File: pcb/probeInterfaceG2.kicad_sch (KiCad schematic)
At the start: 41 parts

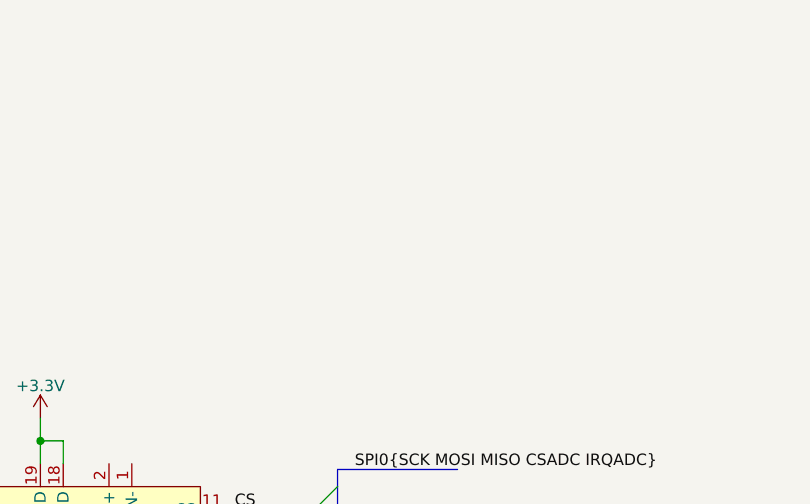
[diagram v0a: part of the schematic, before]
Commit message: Added some design hints
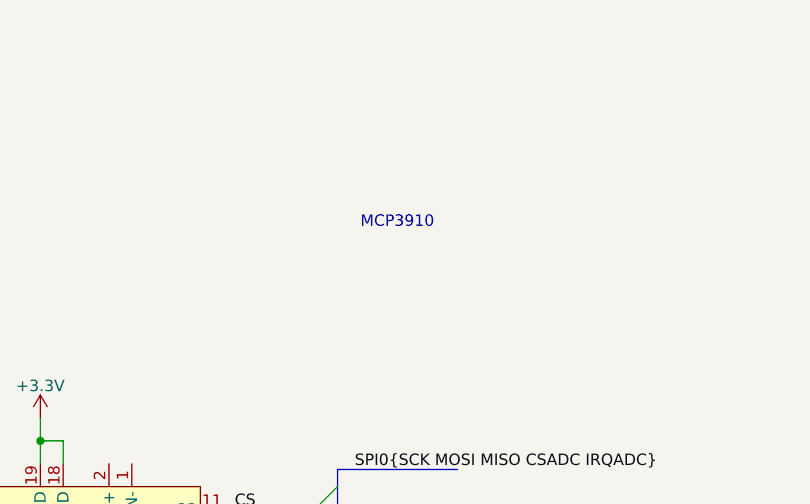
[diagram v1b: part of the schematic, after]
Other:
- note added: "MCP3910"

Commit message: updated schematics for bipolar supply of opamps
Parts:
- removed C?: 100n, symbol Device:C
- removed C? (x2): 220n, symbol Device:C
- removed R? (x2): 220, symbol Device:R
- removed U? (x5): 74HCT4052, symbol Analog_Switch:CD4052B
- removed U? (x2): 74HC595, symbol 74xx:74HC595
- removed U? (x3): LM358, symbol Amplifier_Operational:LM358
- added C?: 1n, symbol Device:C
- added C?: NM, symbol Device:C
- added C?: 100n, symbol Device:C
- added D?: BAV99, Package_TO_SOT_SMD:SOT-23, symbol Diode:BAV99
- added J? (x4): Conn_01x12, symbol Connector_Generic:Conn_01x12
- added M?: SUN MF30060V2-1, symbol Motor:Fan
- added R? (x4): 10k, symbol Device:R
- added R? (x2): 470, symbol Device:R
- added R?: 220, symbol Device:R
- added R?: 82, symbol Device:R
- added RN? (x4): 10k 0.05%, symbol Device:R_Pack04_Split
- added U?: W5500, Package_QFP:LQFP-48_7x7mm_P0.5mm, symbol Interface_Ethernet:W5500
- added U? (x4): OP07, symbol Amplifier_Operational:OP07
- added U?: TL431D, Package_SO:SOIC-8_3.9x4.9mm_P1.27mm, symbol Reference_Voltage:TL431D
- added U?: LM7910_TO220, Package_TO_SOT_THT:TO-220-3_Vertical, symbol Regulator_Linear:LM7910_TO220
- added U? (x2): LM358, symbol Amplifier_Operational:LM358
- added U?: SN74AXC1T45, symbol zz_Logic_LevelTranslator:SN74AXC1T45
- added U?: LM7810_TO220, Package_TO_SOT_THT:TO-220-3_Vertical, symbol Regulator_Linear:LM7810_TO220
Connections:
- net +3.3V: now also U?.1 (VCCA)
- net GND: now also C?.2, D?.2 (A), J?.2, R?.2, C?.2, C?.2, J?.1 (Pin_1), J?.10 (Pin_10), J?.11 (Pin_11), J?.12 (Pin_12), J?.2 (Pin_2), J?.3 (Pin_3), J?.4 (Pin_4), J?.5 (Pin_5), J?.6 (Pin_6), J?.7 (Pin_7), J?.8 (Pin_8), J?.9 (Pin_9), R?.2, U?.1 (GND), U?.2 (A), U?.2 (GND), U?.2 (GND), U?.3 (+), U?.3 (+), U?.3 (A), U?.5 (+), U?.6 (A), U?.7 (A)
- net PP1: now also J?.1 (Pin_1)
- net PP10: now also J?.10 (Pin_10)
- net PP11: now also J?.11 (Pin_11)
- net PP12: now also J?.12 (Pin_12)
- net PP2: now also J?.2 (Pin_2)
- net PP3: now also J?.3 (Pin_3)
- net PP4: now also J?.4 (Pin_4)
- net PP5: now also J?.5 (Pin_5)
- net PP6: now also J?.6 (Pin_6)
- net PP7: now also J?.7 (Pin_7)
- net PP8: now also J?.8 (Pin_8)
- net PP9: now also J?.9 (Pin_9)
- net VS: now reaches D?.1 (K), J?.1, U?.3 (VI)
- new net: U?.11 (AVDD), U?.15 (AVDD), U?.17 (AVDD), U?.21 (AVDD), U?.4 (AVDD), U?.8 (AVDD)
- new net: U?.14 (AGND), U?.16 (AGND), U?.19 (AGND), U?.3 (AGND), U?.48 (AGND), U?.9 (AGND)
- new net: C?.1, C?.1, D?.3 (K), R?.1, R?.2, U?.1 (K), U?.6 (VCCB), U?.7
- new net: R?.1, R?.2, U?.2 (-)
- new net: R?.1, R?.2, U?.6 (-)
- new net: R?.1, R?.2, U?.8 (REF)
- new net: RN?.8 (R1.2), U?.2 (-), U?.6
- new net: C?.1, D?.1 (K), R?.1, U?.4 (B)
- new net: RN?.4 (R4.1), U?.6
- new net: RN?.2 (R2.1), RN?.5 (R4.2), U?.2 (-)
- new net: RN?.7 (R2.2), U?.2 (-), U?.6
- new net: RN?.1 (R1.1), RN?.6 (R3.2), U?.2 (-)
- new net: RN?.3 (R3.1), U?.6
- new net: R?.2, U?.1
- new net: R?.2, U?.3 (A)
- new net +15V: U?.1 (VI)
- new net -15V: U?.2 (VI)
- new net A1: J?.1 (Pin_1)
- new net A10: J?.10 (Pin_10)
- new net A11: J?.11 (Pin_11)
- new net A12: J?.12 (Pin_12)
- new net A2: J?.2 (Pin_2)
- new net A3: J?.3 (Pin_3)
- new net A4: J?.4 (Pin_4)
- new net A5: J?.5 (Pin_5)
- new net A6: J?.6 (Pin_6)
- new net A7: J?.7 (Pin_7)
- new net A8: J?.8 (Pin_8)
- new net A9: J?.9 (Pin_9)
- new net CV REF: R?.1
- new net D1: J?.1 (Pin_1)
- new net D10: J?.10 (Pin_10)
- new net D11: J?.11 (Pin_11)
- new net D12: J?.12 (Pin_12)
- new net D2: J?.2 (Pin_2)
- new net D3: J?.3 (Pin_3)
- new net D4: J?.4 (Pin_4)
- new net D5: J?.5 (Pin_5)
- new net D6: J?.6 (Pin_6)
- new net D7: J?.7 (Pin_7)
- new net D8: J?.8 (Pin_8)
- new net D9: J?.9 (Pin_9)
- new net data: R?.1
- new net dir: U?.5 (DIR)
- new net vn: U?.3 (VO), U?.4 (V-), U?.4 (V-), U?.4 (V-), U?.4 (V-)
- new net vp: U?.3 (VO), U?.7 (V+), U?.7 (V+), U?.7 (V+), U?.7 (V+)
- no-connect marks 3 -> 4
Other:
- removed sheet driver
- removed sheet driver1
- added sheet board1 (board.kicad_sch)
- note added: "AD7172-2"
- note added: "LT1634B MAX6126"
- note added: "Phoenix contact terminal"
- note added: "Traco TMA0515D"
- note added: "check time constant of input res with this cap to be within tl431"
- note added: "jumper field"
- note added: "or capacitance multiplier"
- note added: "protect IOs if wrong direction"
- note removed: "74HC4052"
- note removed: "TODO noninverting amplify to 3.5V"
- moved on the sheet: C?, D?, J?, R?, U?

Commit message: dropped psu part for simpler digital board, schematic and layout almost done
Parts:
- removed C?: 1n, symbol Device:C
- removed C?: 10u, symbol Device:C
- removed C?: NM, symbol Device:C
- removed C? (x2): C, symbol Device:C
- removed C?: 100n, symbol Device:C
- removed D?: D, symbol Device:D
- removed D?: BAV99, Package_TO_SOT_SMD:SOT-23, symbol Diode:BAV99
- removed J? (x4): Conn_01x12, symbol Connector_Generic:Conn_01x12
- removed J?: Conn_02x07_Odd_Even, symbol Connector_Generic:Conn_02x07_Odd_Even
- removed J?: RB1-125B8G1A, Connector_RJ:RJ45_UDE_RB1-125B8G1A, symbol Connector:RB1-125B8G1A
- removed J?: Barrel_Jack, symbol Connector:Barrel_Jack
- removed J?: USB_B_Mini, symbol Connector:USB_B_Mini
- removed M?: SUN MF30060V2-1, symbol Motor:Fan
- removed R? (x6): R, symbol Device:R
- removed R? (x4): 10k, symbol Device:R
- removed R? (x2): 470, symbol Device:R
- removed R? (x2): 4.99k .01%, symbol Device:R
- removed R?: 220, symbol Device:R
- removed R? (x2): 22, symbol Device:R
- removed R?: 82, symbol Device:R
- removed RN? (x4): 10k 0.05%, symbol Device:R_Pack04_Split
- removed U?: W5500, Package_QFP:LQFP-48_7x7mm_P0.5mm, symbol Interface_Ethernet:W5500
- removed U?: DAC8562, symbol zz_AnalogDAC:DAC8562
- removed U?: LT1117-3.3, symbol Regulator_Linear:LT1117-3.3
- removed U?: RP2040, RP2040_minimal:RP2040-QFN-56, symbol zz_MCU_RaspberryPi_RP2040:RP2040
- removed U? (x4): OP07, symbol Amplifier_Operational:OP07
- removed U?: TL431D, Package_SO:SOIC-8_3.9x4.9mm_P1.27mm, symbol Reference_Voltage:TL431D
- removed U?: ADR4540, Package_SO:SOIC-8_3.9x4.9mm_P1.27mm, symbol Reference_Voltage:ADR4540
- removed U?: LM7910_TO220, Package_TO_SOT_THT:TO-220-3_Vertical, symbol Regulator_Linear:LM7910_TO220
- removed U? (x2): LM358, symbol Amplifier_Operational:LM358
- removed U?: LM317_TO-220, Package_TO_SOT_THT:TO-220-3_Vertical, symbol Regulator_Linear:LM317_TO-220
- removed U?: ENC28J60x-ML, Package_DFN_QFN:QFN-28-1EP_6x6mm_P0.65mm_EP4.25x4.25mm, symbol Interface_Ethernet:ENC28J60x-ML
- removed U?: SN74AVC8T245PW, Package_SO:TSSOP-24_4.4x7.8mm_P0.65mm, symbol Logic_LevelTranslator:SN74AVC8T245PW
- removed U?: SN74AXC1T45, symbol zz_Logic_LevelTranslator:SN74AXC1T45
- removed U?: LM7810_TO220, Package_TO_SOT_THT:TO-220-3_Vertical, symbol Regulator_Linear:LM7810_TO220
- removed U?: MCP3562, symbol zz_AnalogADC:MCP3562
- added C1, C17, C4: 10u, Capacitor_SMD:C_0805_2012Metric, symbol Device:C
- added C10, C18, C26, C8: 1u, Capacitor_SMD:C_0402_1005Metric, symbol Device:C
- added C11, C12, C13, C14, C15, C16, C20, C21, C28, C29, C34, C35, C40, C41, C42, C43, C44, C45, C46, C47, C5, C6, C7, C9: 100n, Capacitor_SMD:C_0402_1005Metric, symbol Device:C
- added C19: 100p, Capacitor_SMD:C_0402_1005Metric, symbol Device:C
- added C2, C3: 14p, Capacitor_SMD:C_0402_1005Metric, symbol Device:C
- added C27: 1000p, Capacitor_SMD:C_0402_1005Metric, symbol Device:C
- added D2, D7: BAT54S, Package_TO_SOT_SMD:SOT-23, symbol Diode:BAT54S
- added D4, D5: LED, LED_SMD:LED_0402_1005Metric, symbol Device:LED
- added D40: BZX84C3V6, Package_TO_SOT_SMD:SOT-23, symbol Diode:BZX84Cxx
- added F1: Polyfuse 500mA, Fuse:Fuse_1206_3216Metric, symbol Device:Polyfuse
- added F2: 1A slow, Fuse:Fuse_1206_3216Metric, symbol Device:Fuse
- added HS1: 1455J1201, case:1455J1201, symbol Mechanical:Heatsink_Pad
- added J2: Conn_02x01, Connector_PinSocket_2.54mm:PinSocket_1x02_P2.54mm_Vertical, symbol Connector_Generic:Conn_02x01
- added J3: USB_B, Connector_USB:USB_B_OST_USB-B1HSxx_Horizontal, symbol Connector:USB_B
- added J4: Debug, Connector_PinHeader_2.54mm:PinHeader_1x03_P2.54mm_Vertical, symbol Connector:Conn_01x03_Pin
- added J?: Conn_02x07_Odd_Even, Connector_IDC:IDC-Header_2x07_P2.54mm_Horizontal, symbol Connector_Generic:Conn_02x07_Odd_Even
- added Q1, Q5: BCX56, Package_TO_SOT_SMD:SOT-89-3, symbol Transistor_BJT:BCX56
- added Q3: X0202NN, Package_TO_SOT_SMD:SOT-223, symbol Triac_Thyristor:X0202NN
- added R1, R5: 1k, Capacitor_SMD:C_0402_1005Metric, symbol Device:R
- added R10, R11, R12, R13, R14, R15, R16, R17, R18, R19, R20, R21, R22, R23, R24, R25, R26, R27, R28, R29, R34, R36, R37, R38, R39, R6, R7, R77, R78, R8, R9: 10k, Resistor_SMD:R_0402_1005Metric, symbol Device:R
- added R2: 10k, Capacitor_SMD:C_0402_1005Metric, symbol Device:R
- added R3, R4: 27, Capacitor_SMD:C_0402_1005Metric, symbol Device:R
- added R30: 10R, Resistor_SMD:R_0805_2012Metric, symbol Device:R
- added R31: 100R, Resistor_SMD:R_0402_1005Metric, symbol Device:R
- added R42, R45, R48, R51, R54, R57, R60, R63, R66, R69, R71, R72: 820, Resistor_SMD:R_0402_1005Metric, symbol Device:R
- added R73, R74, R75, R76: 24R, Resistor_SMD:R_0402_1005Metric, symbol Device:R
- added SW1: SW_Push, Button_Switch_THT:SW_Tactile_SPST_Angled_PTS645Vx58-2LFS, symbol Switch:SW_Push
- added SYM1: SYM_Flash_Small, Symbol:Symbol_Highvoltage_Type1_CopperTop_Small, symbol Graphic:SYM_Flash_Small
- added TP1, TP2, TP3, TP4, TP5, TP6, TP7: TestPoint, TestPoint:TestPoint_Bridge_Pitch2.54mm_Drill1.0mm, symbol Connector:TestPoint
- added U1: NCP1117-3.3_SOT223, Package_TO_SOT_SMD:SOT-223-3_TabPin2, symbol Regulator_Linear:NCP1117-3.3_SOT223
- added U13, U18, U6: SN74AXC4T774RSVR, levelShifter:XQFN16, symbol levelShifter:SN74AVC4T774GUX
- added U2: W25Q128JVS, Package_SO:SOIC-8_5.23x5.23mm_P1.27mm, symbol Memory_Flash:W25Q128JVS
- added U23: RP2040, Package_DFN_QFN:QFN-56-1EP_7x7mm_P0.4mm_EP3.2x3.2mm_ThermalVias, symbol MCU_RaspberryPi:RP2040
- added U24: TBA 1-0511, Converter_DCDC:Converter_DCDC_Murata_CRE1xxxxxx3C_THT, symbol dcdcConverter:TBA_1-0511
- added U25: TBA 2-0511, Converter_DCDC:Converter_DCDC_TRACO_TMR-1-xxxx_Single_THT, symbol dcdcConverter:TBA_2-0511
- added U3: ADUM3160, Package_SO:SOIC-16W_7.5x10.3mm_P1.27mm, symbol Interface_USB:ADUM3160
- added U4, U5, U9: 74HCT595, Package_SO:SO-16_3.9x9.9mm_P1.27mm, symbol 74xx:74HCT595
- added U7: MCP6002-xSN, Package_SO:SOIC-8_3.9x4.9mm_P1.27mm, symbol Amplifier_Operational:MCP6002-xSN
- added Y2: 12.000MHz 12p, Crystal:Crystal_SMD_Abracon_ABM3B-4Pin_5.0x3.2mm, symbol Device:Crystal_GND24
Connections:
- net GND: now also C1.2, C10.2, C11.2, C12.2, C13.2, C14.2, C15.2, C16.2, C17.2, C18.2, C2.2, C20.2, C21.2, C26.2, C27.2, C28.2, C29.2, C3.2, C34.2, C35.2, C4.2, C40.2, C43.2, C44.2, C45.2, C46.2, C47.2, C5.2, C6.2, C7.2, C8.2, C9.2, D2.1 (A), D4.1 (K), D5.1 (K), HS1.1, J2.2 (Pin_2), J4.2 (Pin_2), J?.1 (Pin_1), J?.13 (Pin_13), Q3.1 (K), R31.2, R38.1, R6.2, SW1.1, U1.1 (GND), U13.7 (~{OE}), U13.8 (GND), U13.9 (GND), U18.7 (~{OE}), U18.8 (GND), U18.9 (GND), U2.4 (GND), U23.19 (TESTEN), U23.57 (GND), U24.3 (-Vout), U25.4 (-Vout), U3.15 (GND2), U3.9 (GND2), U4.13 (~{OE}), U4.8 (GND), U5.13 (~{OE}), U5.8 (GND), U6.7 (~{OE}), U6.8 (GND), U6.9 (GND), U7.4 (V-), U9.13 (~{OE}), U9.8 (GND), Y2.2, Y2.4
- net PP1: now also J?.2 (Pin_2)
- net PP10: now also J?.11 (Pin_11)
- net PP11: now also J?.12 (Pin_12)
- net PP12: now also J?.14 (Pin_14)
- net PP2: now also J?.3 (Pin_3)
- net PP3: now also J?.4 (Pin_4)
- net PP4: now also J?.5 (Pin_5)
- net PP5: now also J?.6 (Pin_6)
- net PP6: now also J?.7 (Pin_7)
- net PP7: now also J?.8 (Pin_8)
- net PP8: now also J?.9 (Pin_9)
- net PP9: now also J?.10 (Pin_10)
- new net: C3.1, R5.2, Y2.1
- new net: R3.1, U23.47 (USB_DP)
- new net: R4.1, U23.46 (USB_DM)
- new net: R51.2, U6.4 (A4)
- new net: C27.1, D2.3 (COM), R39.1, U7.5 (+)
- new net: C41.1, F2.2, TP1.1, U24.2 (+Vin), U25.1 (+Vin), U3.1 (VBUS1)
- new net: R22.2, R23.1, R24.1
- new net: R45.2, U6.2 (A2)
- new net: R20.2, R21.1, R22.1
- new net: Q1.1 (B), Q5.3 (E), R30.1, TP7.1
- new net: C19.1, Q1.2 (C), Q5.1 (B), U7.1
- new net: R18.2, R19.1, R20.1
- new net: R24.2, R25.1, R26.1
- new net: R26.2, R27.1, R28.1
- new net: R16.2, R17.1, R18.1
- new net: R66.2, U18.1 (A1)
- new net: R69.2, U18.2 (A2)
- new net: R71.2, U18.3 (A3)
- new net: R72.2, U18.4 (A4)
- new net: R42.2, U6.1 (A1)
- new net: R48.2, U6.3 (A3)
- new net: R37.1, U7.2 (-)
- new net: R10.1, R8.1, R9.2
- new net: D5.2 (A), R77.1, R78.1
- new net: C44.1, U3.12 (PIN), U3.13 (SPD), U3.14 (VDD2)
- new net: R6.1, R7.1, R9.1
- new net: R74.1, U3.11 (DD-)
- new net: C42.1, U3.3 (VDD1), U3.4 (PDEN), U3.5 (SPU)
- new net: C41.2, C42.2, J3.4 (GND), J3.5 (Shield), TP2.1, U24.1 (-Vin), U25.2 (-Vin), U3.2 (GND1), U3.8 (GND1)
- new net: F1.2, U24.4 (+Vout), U25.6 (+Vout)
- new net: R14.2, R15.1, R16.1
- new net: R12.2, R13.1, R14.1
- new net: D4.2 (A), R34.1, R36.1
- new net: D40.1 (A), Q3.3 (G), R31.1
- new net: F2.1, J3.1 (VBUS)
- new net: R54.2, U13.1 (A1)
- new net: R57.2, U13.2 (A2)
- new net: R60.2, U13.3 (A3)
- new net: R63.2, U13.4 (A4)
- new net: U4.9 (QH'), U5.14 (SER)
- new net: U5.9 (QH'), U9.14 (SER)
- new net: R73.1, U3.10 (DD+)
- new net: R76.2, U3.6 (UD-)
- new net: R75.2, U3.7 (UD+)
- new net: D7.1 (A), U7.7
- new net: R10.2, R11.1, R12.1
- new net: J2.1 (Pin_1), R38.2, R39.2
- new net +1V1: C6.1, C7.1, C8.1, U23.23 (DVDD), U23.45 (VREG_VOUT), U23.50 (DVDD)
- new net +3V3: C10.1, C11.1, C12.1, C13.1, C14.1, C15.1, C16.1, C17.1, C20.1, C28.1, C34.1, C4.1, C45.1, C46.1, C47.1, C5.1, C9.1, D2.2 (K), R2.1, TP4.1, U1.2 (VO), U13.14 (VCCA), U18.14 (VCCA), U2.8 (VCC), U23.1 (IOVDD), U23.10 (IOVDD), U23.22 (IOVDD), U23.33 (IOVDD), U23.42 (IOVDD), U23.43 (ADC_AVDD), U23.44 (VREG_IN), U23.48 (USB_VDD), U23.49 (IOVDD), U4.10 (~{SRCLR}), U4.16 (VCC), U5.10 (~{SRCLR}), U5.16 (VCC), U6.14 (VCCA), U9.10 (~{SRCLR}), U9.16 (VCC)
- new net DAC0: R7.2, U5.3 (QD)
- new net DAC1: R8.2, U5.2 (QC)
- new net DAC10: R27.2, U4.1 (QB)
- new net DAC11: R29.2, U4.15 (QA)
- new net DAC2: R11.2, U5.1 (QB)
- new net DAC3: R13.2, U5.15 (QA)
- new net DAC4: R15.2, U4.7 (QH)
- new net DAC5: R17.2, U4.6 (QG)
- new net DAC6: R19.2, U4.5 (QF)
- new net DAC7: R21.2, U4.4 (QE)
- new net DAC8: R23.2, U4.3 (QD)
- new net DAC9: R25.2, U4.2 (QC)
- new net GPIO0: U18.6 (DIR4), U23.2 (GPIO0)
- new net GPIO1: U18.5 (DIR3), U23.3 (GPIO1)
- new net GPIO10: R63.1, U23.13 (GPIO10)
- new net GPIO11: R60.1, U23.14 (GPIO11)
- new net GPIO12: R57.1, U23.15 (GPIO12)
- new net GPIO13: R54.1, U23.16 (GPIO13)
- new net GPIO14: U13.16 (DIR2), U23.17 (GPIO14)
- new net GPIO15: U13.15 (DIR1), U23.18 (GPIO15)
- new net GPIO16: U23.27 (GPIO16), U6.6 (DIR4)
- new net GPIO17: U23.28 (GPIO17), U6.5 (DIR3)
- new net GPIO18: R51.1, U23.29 (GPIO18)
- new net GPIO19: R48.1, U23.30 (GPIO19)
- new net GPIO2: R72.1, U23.4 (GPIO2)
- new net GPIO20: R45.1, U23.31 (GPIO20)
- new net GPIO21: R42.1, U23.32 (GPIO21)
- new net GPIO22: U23.34 (GPIO22), U6.16 (DIR2)
- new net GPIO23: U23.35 (GPIO23), U6.15 (DIR1)
- new net GPIO24: U23.36 (GPIO24), U4.14 (SER)
- new net GPIO25: U23.37 (GPIO25), U4.12 (RCLK), U5.12 (RCLK), U9.12 (RCLK)
- new net GPIO26: U23.38 (GPIO26_ADC0), U4.11 (SRCLK), U5.11 (SRCLK), U9.11 (SRCLK)
- new net GPIO27: R34.2, R36.2, U23.39 (GPIO27_ADC1)
- new net GPIO28: R77.2, R78.2, U23.40 (GPIO28_ADC2)
- new net GPIO29: U23.41 (GPIO29_ADC3)
- new net GPIO3: R71.1, U23.5 (GPIO3)
- new net GPIO4: R69.1, U23.6 (GPIO4)
- new net GPIO5: R66.1, U23.7 (GPIO5)
- new net GPIO6: U18.16 (DIR2), U23.8 (GPIO6)
- new net GPIO7: U18.15 (DIR1), U23.9 (GPIO7)
- new net GPIO8: U13.6 (DIR4), U23.11 (GPIO8)
- new net GPIO9: U13.5 (DIR3), U23.12 (GPIO9)
- new net K1: U5.7 (QH)
- new net K10: U9.3 (QD)
- new net K11: U9.5 (QF)
- new net K12: U9.4 (QE)
- new net K2: U5.6 (QG)
- new net K3: U9.15 (QA)
- new net K4: U5.5 (QF)
- new net K5: U9.1 (QB)
- new net K6: U5.4 (QE)
- new net K7: U9.7 (QH)
- new net K8: U9.2 (QC)
- new net K9: U9.6 (QG)
- new net QSPI_SCLK: U2.6 (CLK), U23.52 (QSPI_SCLK)
- new net QSPI_SD0: U2.5 (DI(IO0)), U23.53 (QSPI_SD0)
- new net QSPI_SD1: U2.2 (DO(IO1)), U23.55 (QSPI_SD1)
- new net QSPI_SD2: U2.3 (IO2), U23.54 (QSPI_SD2)
- new net QSPI_SD3: U2.7 (IO3), U23.51 (QSPI_SD3)
- new net QSPI_SS: R1.1, R2.2, U2.1 (~{CS}), U23.56 (QSPI_SS)
- new net RUN: U23.26 (RUN)
- new net SWCLK: J4.1 (Pin_1), U23.24 (SWCLK)
- new net SWDIO: J4.3 (Pin_3), U23.25 (SWD)
- new net USB_D+: R3.2, R73.2
- new net USB_D-: R4.2, R74.2
- new net USBi_D+: J3.3 (D+), R75.1
- new net USBi_D-: J3.2 (D-), R76.1
- new net VBUS: C1.1, C26.1, C40.1, C43.1, F1.1, Q5.2 (C), TP3.1, U1.3 (VI), U3.16 (VBUS2), U7.8 (V+)
- new net VDD: C18.1, C19.2, C21.1, C29.1, C35.1, D40.3 (K), Q1.3 (E), Q3.2 (A), Q3.4 (A), R30.2, R37.2, TP6.1, U13.13 (VCCB), U18.13 (VCCB), U6.13 (VCCB)
- new net XIN: C2.1, U23.20 (XIN), Y2.3
- new net XOUT: R5.1, U23.21 (XOUT)
- new net dacout: D7.3 (COM), R28.2, R29.1, TP5.1, U7.3 (+), U7.6 (-)
- new net io1/int: U6.12 (B1)
- new net io10/int: U18.11 (B2)
- new net io11/int: U18.10 (B3)
- new net io12/int: U18.9 (GND)
- new net io2/int: U6.11 (B2)
- new net io3/int: U6.10 (B3)
- new net io4/int: U6.9 (GND)
- new net io5/int: U13.12 (B1)
- new net io6/int: U13.11 (B2)
- new net io7/int: U13.10 (B3)
- new net io8/int: U13.9 (GND)
- new net io9/int: U18.12 (B1)
- new net ~{USB_BOOT}: R1.2, SW1.2
- no-connect marks 4 -> 1
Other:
- removed sheet board1
- added sheet io1 (io.kicad_sch)
- added sheet io10 (io.kicad_sch)
- added sheet io11 (io.kicad_sch)
- added sheet io12 (io.kicad_sch)
- added sheet io2 (io.kicad_sch)
- added sheet io3 (io.kicad_sch)
- added sheet io4 (io.kicad_sch)
- added sheet io5 (io.kicad_sch)
- added sheet io6 (io.kicad_sch)
- added sheet io7 (io.kicad_sch)
- added sheet io8 (io.kicad_sch)
- added sheet io9 (io.kicad_sch)
- note added: "14p for 12p crystal 27p for 18p crystal"
- note added: "2x SEB 2610F"
- note added: "Crystal"
- note added: "Flash"
- note added: "Make sure C10 is close to pin 44 of RP2040"
- note added: "Make sure C8 is close to pin 45 of RP2040"
- note added: "Make sure R3 and R4 are close to RP2040"
- note added: "Power"
- note removed: "2*4+1 (SPI) + (2*)5 (mux) + 12 (data) + 3*12"
- note removed: "74AVC1T45 SN74AXC1T45"
- note removed: "AD7172-2"
- note removed: "ADS131A02"
- note removed: "DAC8551 DAC8411"
- note removed: "DAC8562"
- note removed: "HR911105A"
- note removed: "LT1021"
- note removed: "LT1634B MAX6126"
- note removed: "MCP3562"
- note removed: "MCP3910"
- note removed: "Phoenix contact terminal"
- note removed: "TI part not Analog"
- note removed: "Traco TMA0515D"
- note removed: "check time constant of input res with this cap to be within tl431"
- note removed: "internal USB for programming only, no galvanic isolation"
- note removed: "jumper field"
- note removed: "low voltage noise supply: ~ 0-8v high gain ADA4522 OPAx227"
- note removed: "or capacitance multiplier"
- note removed: "protect IOs if wrong direction"
- note removed: "slow gpios: direction digitalSwitch short (CC) fast gpios: digital data"
- company: (none) -> M. Koch
- title: (none) -> LTE probeInterfaceG2

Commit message: layout done
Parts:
- added C48: 10u, Capacitor_SMD:C_0805_2012Metric, symbol Device:C
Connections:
- net GND: now also C48.2
- net VBUS: now also C48.1
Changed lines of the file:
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@@
   (junction (at 64.77 34.29) (diameter 0) (color 0 0 0 0)
   )
+  (junction (at 354.33 280.67) (diameter 0) (color 0 0 0 0)
+  )
   (junction (at 480.06 209.55) (diameter 0) (color 0 0 0 0)
   )
@@
     (stroke (width 0) (type default))
   )
+  (wire (pts (xy 364.49 288.29) (xy 364.49 289.56))
+    (stroke (width 0) (type default))
+  )
   (wire (pts (xy 336.55 40.64) (xy 336.55 39.37))
     (stroke (width 0) (type default))
@@
     (stroke (width 0) (type default))
   )
+  (wire (pts (xy 354.33 280.67) (xy 364.49 280.67))
+    (stroke (width 0) (type default))
+  )
   (wire (pts (xy 210.82 246.38) (xy 210.82 247.65))
     (stroke (width 0) (type default))
@@
     (stroke (width 0) (type default))
   )
-  (wire (pts (xy 354.33 279.4) (xy 354.33 293.37))
+  (wire (pts (xy 354.33 279.4) (xy 354.33 280.67))
     (stroke (width 0) (type default))
   )
@@
     (stroke (width 0) (type default))
   )
+  (wire (pts (xy 354.33 280.67) (xy 354.33 293.37))
+    (stroke (width 0) (type default))
+  )
   (wire (pts (xy 66.04 275.59) (xy 66.04 276.86))
     (stroke (width 0) (type default))
@@
     )
   )
+  (symbol (lib_id "power:GND") (at 364.49 289.56 0) (unit 1)
+    (in_bom yes) (on_board yes) (dnp no)
+    (property "Reference" "#PWR0128" (at 364.49 295.91 0)
+      (effects (font (size 1.27 1.27)) hide)
+    )
+    (property "Value" "GND" (at 360.68 290.83 0)
+      (effects (font (size 1.27 1.27)))
+    )
+    (property "Footprint" "" (at 364.49 289.56 0)
+      (effects (font (size 1.27 1.27)) hide)
+    )
+    (property "Datasheet" "" (at 364.49 289.56 0)
+      (effects (font (size 1.27 1.27)) hide)
+    )
+    (pin "1")
+    (instances
+      (project "probeInterfaceG2"
+        (path "/6ffd737b-9cf1-4f67-98df-7cc1cbeaaab7"
+          (reference "#PWR0128") (unit 1)
+        )
+      )
+    )
+  )
   (symbol (lib_id "Device:C") (at 336.55 209.55 0) (unit 1)
     (in_bom yes) (on_board yes) (dnp no) (fields_autoplaced)
@@
         )
       )
+    )
+  )
+  (symbol (lib_id "Device:C") (at 364.49 284.48 0) (unit 1)
+    (in_bom yes) (on_board yes) (dnp no)
+    (property "Reference" "C48" (at 367.411 283.3116 0)
+      (effects (font (size 1.27 1.27)) (justify left))
+    )
+    (property "Value" "10u" (at 367.411 285.623 0)
+      (effects (font (size 1.27 1.27)) (justify left))
+    )
+    (property "Footprint" "Capacitor_SMD:C_0805_2012Metric" (at 365.4552 288.29 0)
+      (effects (font (size 1.27 1.27)) hide)
+    )
+    (property "Datasheet" "~" (at 364.49 284.48 0)
+      (effects (font (size 1.27 1.27)) hide)
+    )
+    (pin "1")
+    (pin "2")
+    (instances
+      (project "probeInterfaceG2"
+        (path "/6ffd737b-9cf1-4f67-98df-7cc1cbeaaab7"
+          (reference "C48") (unit 1)
+        )
+      )

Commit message: fixed drc
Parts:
- U23: footprint Package_DFN_QFN:QFN-56-1EP_7x7mm_P0.4mm_EP3.2x3.2mm_ThermalVias -> Package_DFN_QFN:QFN-56-1EP_7x7mm_P0.4mm_EP3.2x3.2mm
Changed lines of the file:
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@@
       (effects (font (size 1.27 1.27)) (justify left))
     )
-    (property "Footprint" "Package_DFN_QFN:QFN-56-1EP_7x7mm_P0.4mm_EP3.2x3.2mm_ThermalVias" (at 317.5 118.11 0)
+    (property "Footprint" "Package_DFN_QFN:QFN-56-1EP_7x7mm_P0.4mm_EP3.2x3.2mm" (at 317.5 118.11 0)
       (effects (font (size 1.27 1.27)) hide)
     )

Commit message: reichelt bom added
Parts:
- C1, C17, C4, C48: Reichelt (none) -> X5R-G0805 10/16
- C10, C18, C26, C8: Reichelt (none) -> MUR GRM155R61A47
- C11, C12, C13, C14, C15, C16, C20, C21, C28, C29, C34, C35, C40, C41, C42, C43, C44, C45, C46, C47, C5, C6, C7, C9: Reichelt (none) -> WAL 0402B104K500
- C19: Reichelt (none) -> RND 150MT15N1012
- C2, C3: Reichelt (none) -> RND 150C0402N18
- C27: Reichelt (none) -> MUR GRM1555C1H10
- D2, D7: Reichelt (none) -> BAT 54S DIO
- D4: value LED -> LED gr; Reichelt (none) -> EVL 16-213UYC
- D40: Reichelt (none) -> SMD ZD 3,6
- D5: value LED -> LED rd; Reichelt (none) -> EVL 16-213USRC
- HS1: Reichelt (none) -> 1455J1201
- J3: Reichelt (none) -> USB BW
- J?: Reichelt (none) -> WSL 14W
- Q1, Q5: Reichelt (none) -> BCX 56-16 NXP
- Q3: Reichelt (none) -> BT 148W-600R NXP
- R1, R5: Reichelt (none) -> RND 155HP02 AB
- R10, R11, R12, R13, R14, R15, R16, R17, R18, R19, R20, R21, R22, R23, R24, R25, R26, R27, R28, R29, R34, R36, R37, R38, R39, R6, R7, R77, R78, R8, R9: Reichelt (none) -> RND 155HP02 AC
- R2: footprint Capacitor_SMD:C_0402_1005Metric -> Resistor_SMD:R_0402_1005Metric; Reichelt (none) -> RND 155HP02 AC
- R3, R4: value 27 -> 27R; footprint Capacitor_SMD:C_0402_1005Metric -> Resistor_SMD:R_0402_1005Metric; Reichelt (none) -> RND 0402 1 27
- R30: Reichelt (none) -> RND 155HP05 AF
- R31: Reichelt (none) -> RND 0402 1 100
- R42, R45, R48, R51, R54, R57, R60, R63, R66, R69, R71, R72: Reichelt (none) -> RND 0402 1 820
- R73, R74, R75, R76: Reichelt (none) -> RND 155HP02 BY
- TP1, TP3, TP4, TP5, TP7: now left out of the parts list
- U1: Reichelt (none) -> TS 1117 BCW33
- U23: Reichelt (none) -> RPI RP2040
- U24: Reichelt (none) -> TBA 1-0511
- U25: Reichelt (none) -> TBA 2-0511
- U3: Reichelt (none) -> ADUM 3160
- U4, U5, U9: Reichelt (none) -> SMD HC 595
- U7: Reichelt (none) -> MCP 6002-I/SN

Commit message: added digikey bom
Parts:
- C1, C17, C4, C48: Digikey (none) -> 1276-1096-1-ND
- C10, C18, C26, C8: Digikey (none) -> 1276-1076-1-ND
- C11, C12, C13, C14, C15, C16, C20, C21, C28, C29, C34, C35, C40, C41, C42, C43, C44, C45, C46, C47, C5, C6, C7, C9: Digikey (none) -> 1276-1043-1-ND
- C19: Digikey (none) -> 13-CC0402JPNPO9BN101DKR-ND
- C2, C3: Digikey (none) -> 13-CC0402JPNPO9BN180DKR-ND
- C27: Digikey (none) -> 490-GCM1555C1H102GA16JDKR-ND
- D2, D7: Digikey (none) -> BAT54SLT1GOSDKR-ND
- D4: Digikey (none) -> 754-1101-1-ND
- D40: Digikey (none) -> BZX84C3V6LT1GOSDKR-ND
- D5: Digikey (none) -> 754-1104-1-ND
- F2: Digikey (none) -> 507-1891-1-ND
- HS1: Digikey (none) -> HM890-ND
- J3: Digikey (none) -> 102-3999-ND
- J?: Digikey (none) -> S9028-ND
- Q1, Q5: Digikey (none) -> 1727-2930-1-ND
- Q3: Digikey (none) -> 497-7697-1-ND
- R1, R5: Digikey (none) -> 13-AC0402FR-131KLDKR-ND
- R10, R11, R12, R13, R14, R15, R16, R17, R18, R19, R2, R20, R21, R22, R23, R24, R25, R26, R27, R28, R29, R34, R36, R37, R38, R39, R6, R7, R77, R78, R8, R9: Digikey (none) -> YAG3436CT-ND
- R3, R4: Digikey (none) -> YAG3086CT-ND
- R30: Digikey (none) -> 13-RC0402FR-1310RLDKR-ND
- R31: Digikey (none) -> YAG3435CT-ND
- R42, R45, R48, R51, R54, R57, R60, R63, R66, R69, R71, R72: Digikey (none) -> 311-820LRCT-ND
- R73, R74, R75, R76: Digikey (none) -> YAG3073CT-ND
- SW1: Digikey (none) -> PTS645VM58-2 LFS
- U1: Digikey (none) -> AZ1117IH-3.3TRG1DIDKR-ND
- U13, U18, U6: Digikey (none) -> 296-SN74AXC4T774RSVRDKR-ND
- U2: Digikey (none) -> W25Q128JVSIQDKR-ND
- U23: Digikey (none) -> 2648-SC0914(13)DKR-ND
- U24: Digikey (none) -> 1951-3369-ND
- U25: Digikey (none) -> 1951-3429-ND
- U3: Digikey (none) -> ADUM3160BRWZ-RLDKR-ND
- U4, U5, U9: Digikey (none) -> 1727-2821-1-ND
- U7: Digikey (none) -> MCP6002-I/SN-ND
